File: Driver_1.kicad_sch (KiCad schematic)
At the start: 26 parts

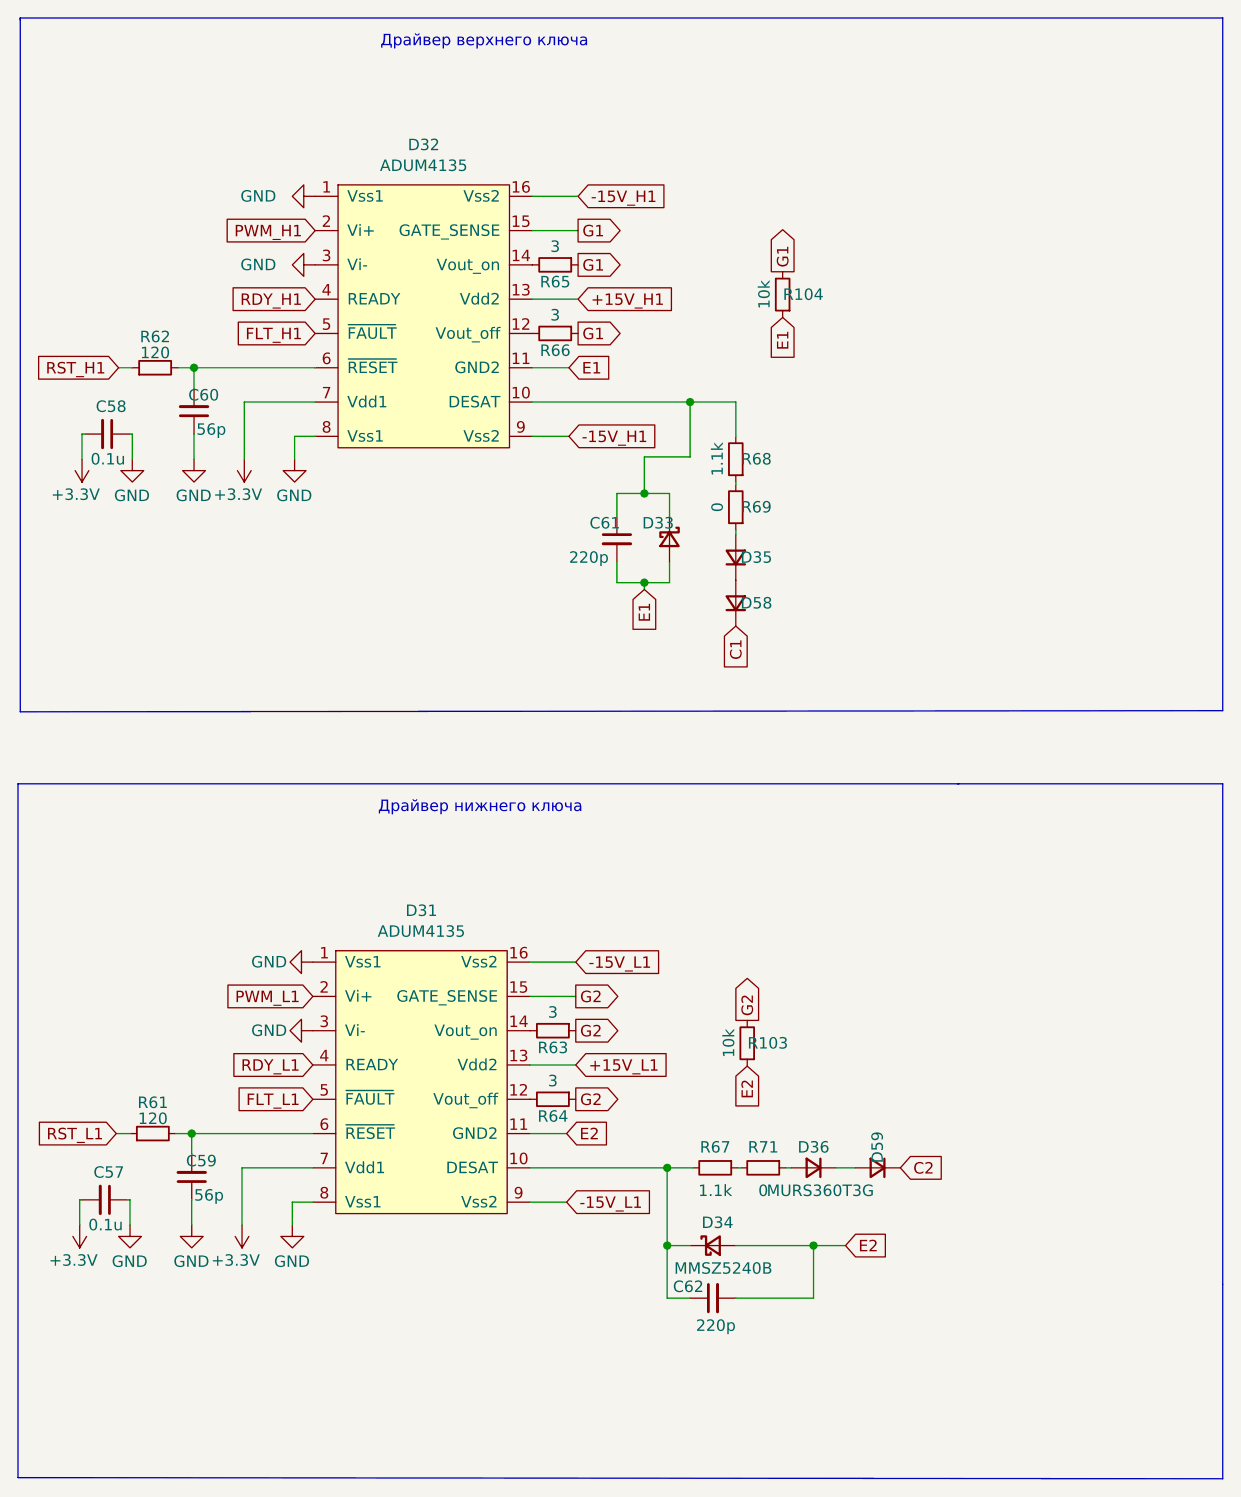
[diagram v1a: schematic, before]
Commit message: Поменял драйвера на китайские
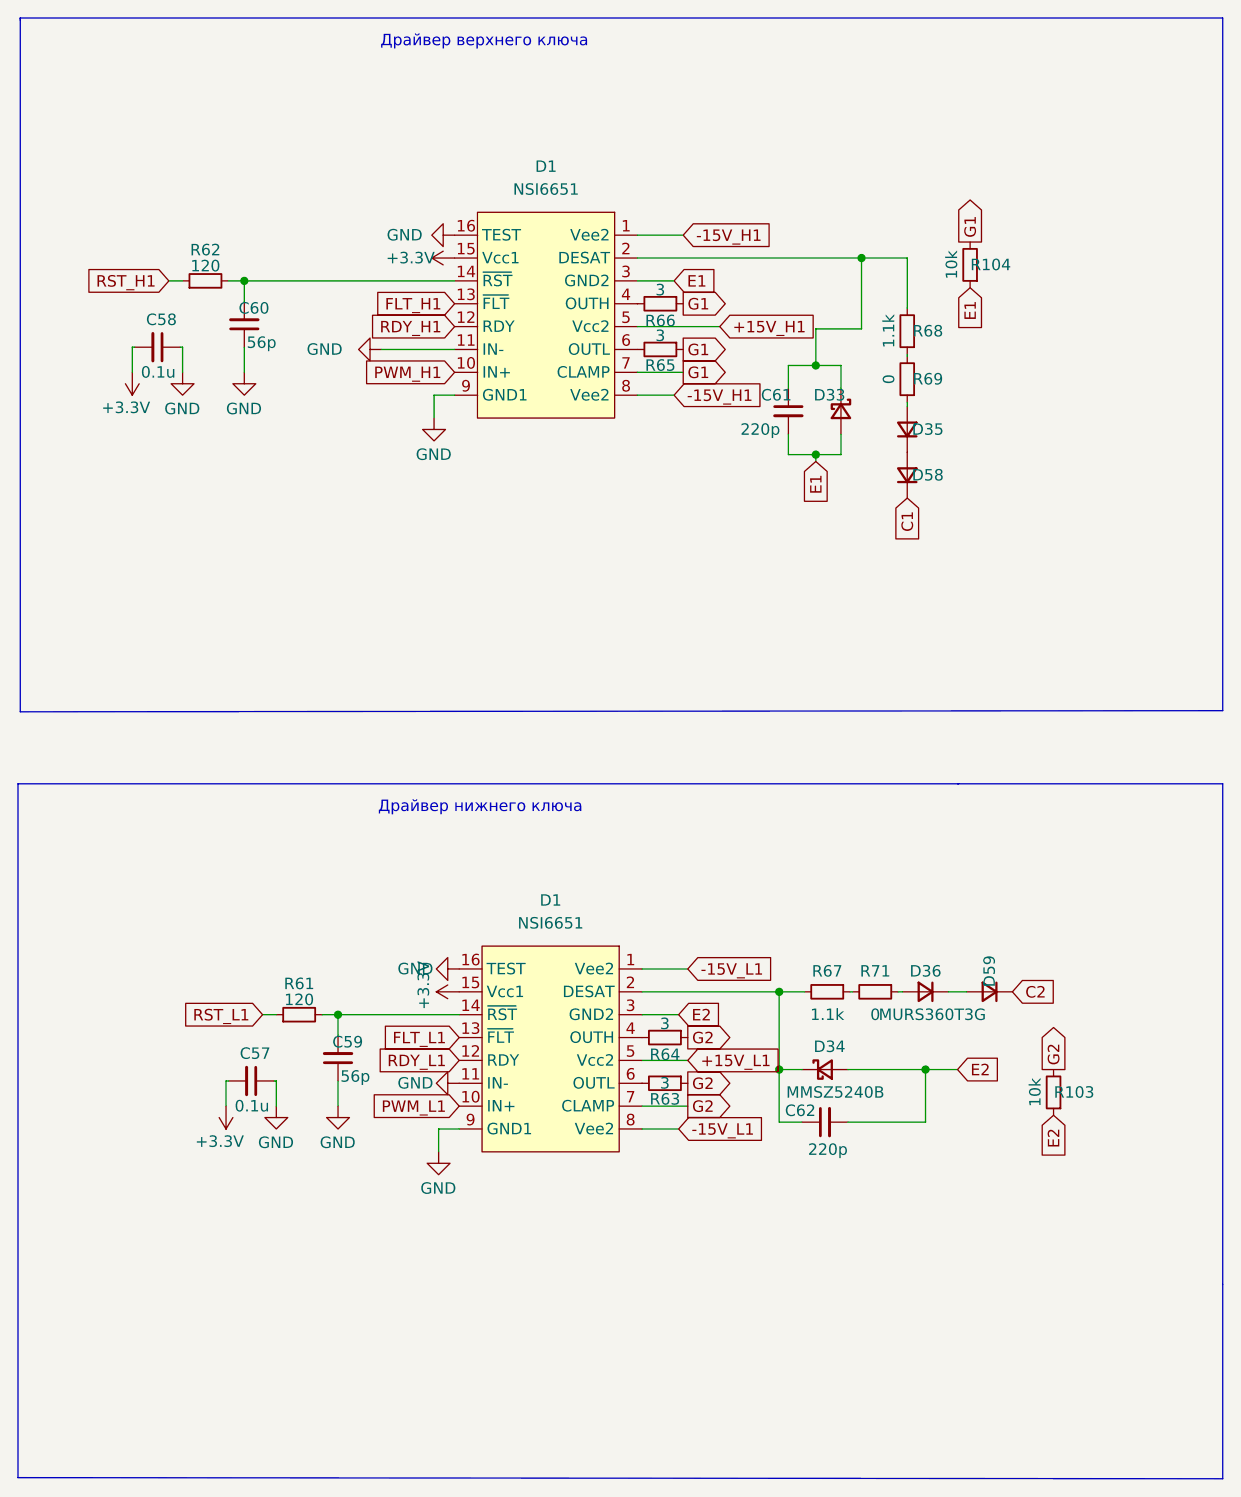
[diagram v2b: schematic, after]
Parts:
- removed D31, D32: ADUM4135, Package_SO:SOIC-16W_7.5x10.3mm_P1.27mm, symbol ADUM_Driver:ADUM4135
- added D1 (x2): NSI6651, Package_SO:SOIC-16W_7.5x10.3mm_P1.27mm, symbol Driver_My:NSI6651
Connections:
- net +15V_H1: now also D1.5 (Vcc2)
- net +15V_L1: now also D1.5 (Vcc2)
- net +3V3: now also D1.15 (Vcc1), D1.15 (Vcc1)
- net -15V_H1: now also D1.1 (Vee2), D1.8 (Vee2)
- net -15V_L1: now also D1.1 (Vee2), D1.8 (Vee2)
- net E1: now also D1.3 (GND2)
- net E2: now also D1.3 (GND2)
- net FLT_H1: now also D1.13 (~{FLT})
- net FLT_L1: now also D1.13 (~{FLT})
- net G1: now also D1.7 (CLAMP)
- net G2: now also D1.7 (CLAMP)
- net GND: now also D1.11 (IN-), D1.11 (IN-), D1.16 (TEST), D1.16 (TEST), D1.9 (GND1), D1.9 (GND1)
- net PWM_H1: now also D1.10 (IN+)
- net PWM_L1: now also D1.10 (IN+)
- net RDY_H1: now also D1.12 (RDY)
- net RDY_L1: now also D1.12 (RDY)
- net at C59.2, R61.2: now also D1.14 (~{RST})
- net at C62.1, D34.1 (K), R67.2: now also D1.2 (DESAT)
- net at R64.2: now also D1.4 (OUTH)
- net at R63.2: now also D1.6 (OUTL)
- net at C61.1, D33.1 (K), R68.2: now also D1.2 (DESAT)
- net at R66.2: now also D1.4 (OUTH)
- net at R65.2: now also D1.6 (OUTL)
- net at C60.2, R62.2: now also D1.14 (~{RST})
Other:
- moved on the sheet: C57, C58, C59, C60, C61, C62, D33, D34, D35, D36, D58, D59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

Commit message: Изменил схему
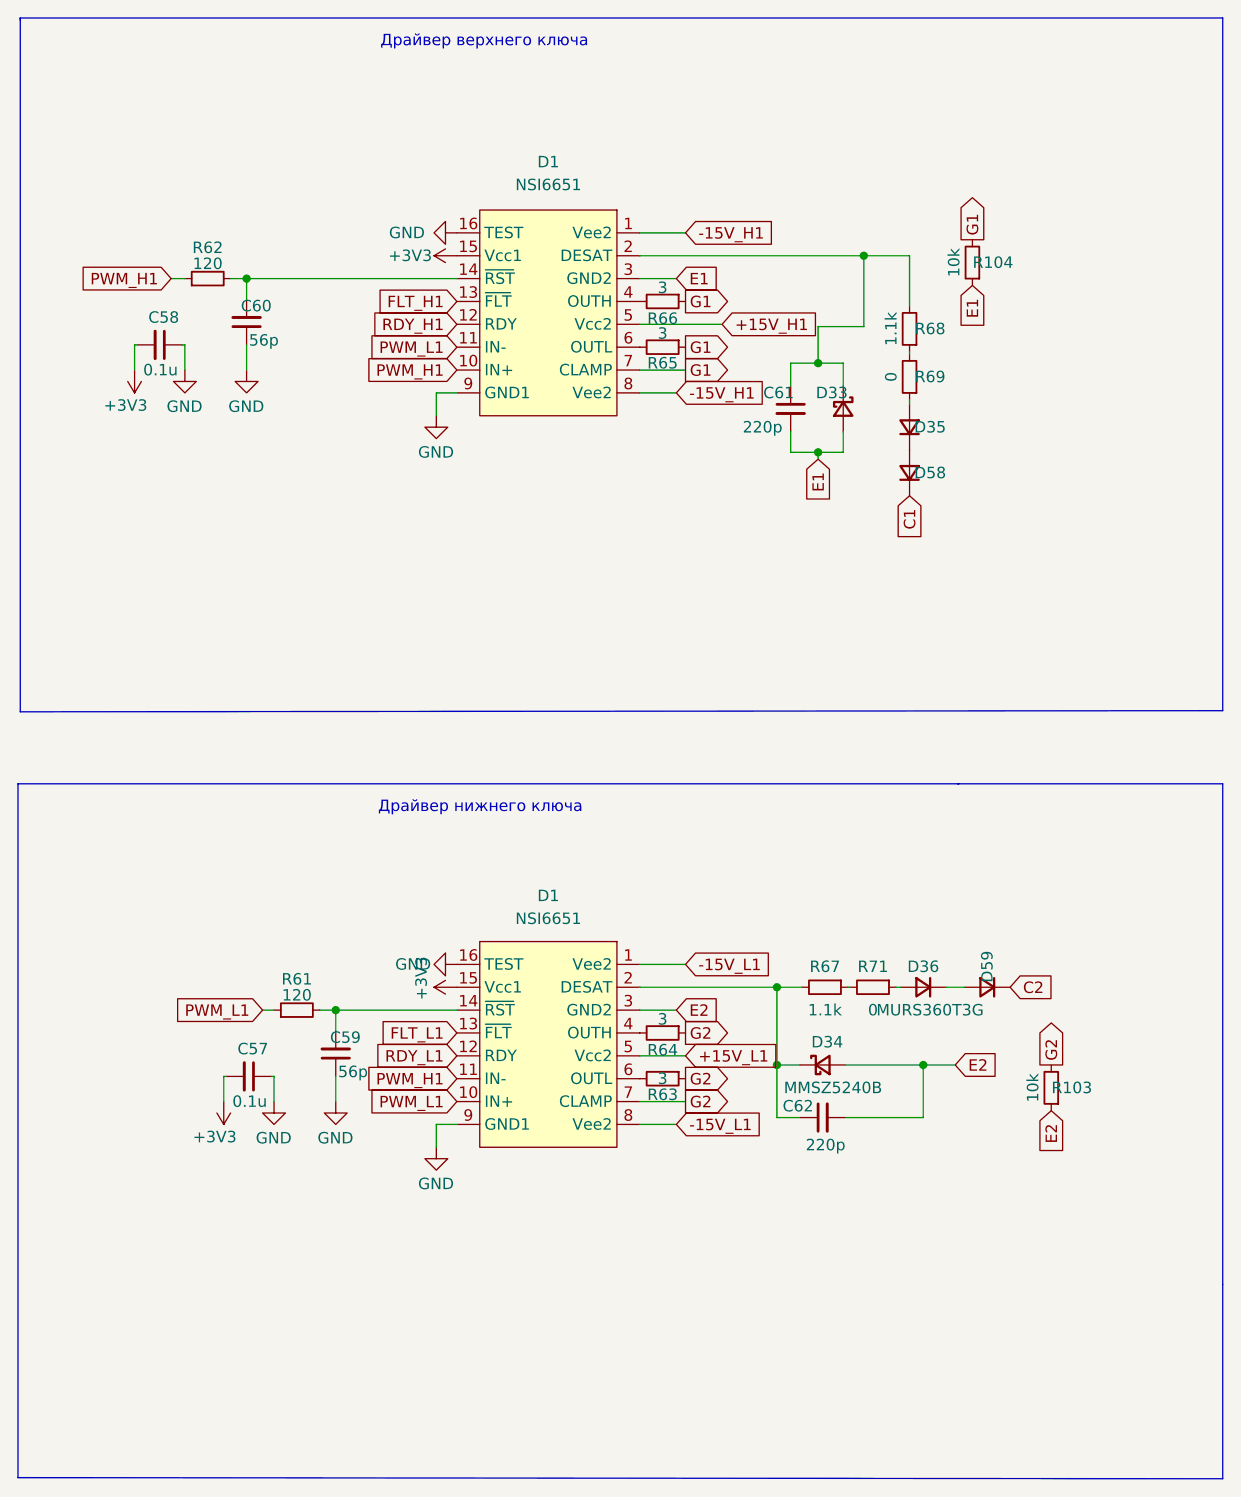
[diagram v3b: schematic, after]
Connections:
- net RST_H1 is gone; now on net PWM_H1: R62.1
- net RST_L1 is gone; now on net PWM_L1: R61.1
- net GND: no longer D1.11 (IN-), D1.11 (IN-)
- net PWM_H1: now also D1.11 (IN-)
- net PWM_L1: now also D1.11 (IN-)
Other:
- moved on the sheet: C57, C59, C62, D1, D34, D36, D59, R103, R61, R63, R64, R67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

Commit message: Разместил все три стойки в своей области
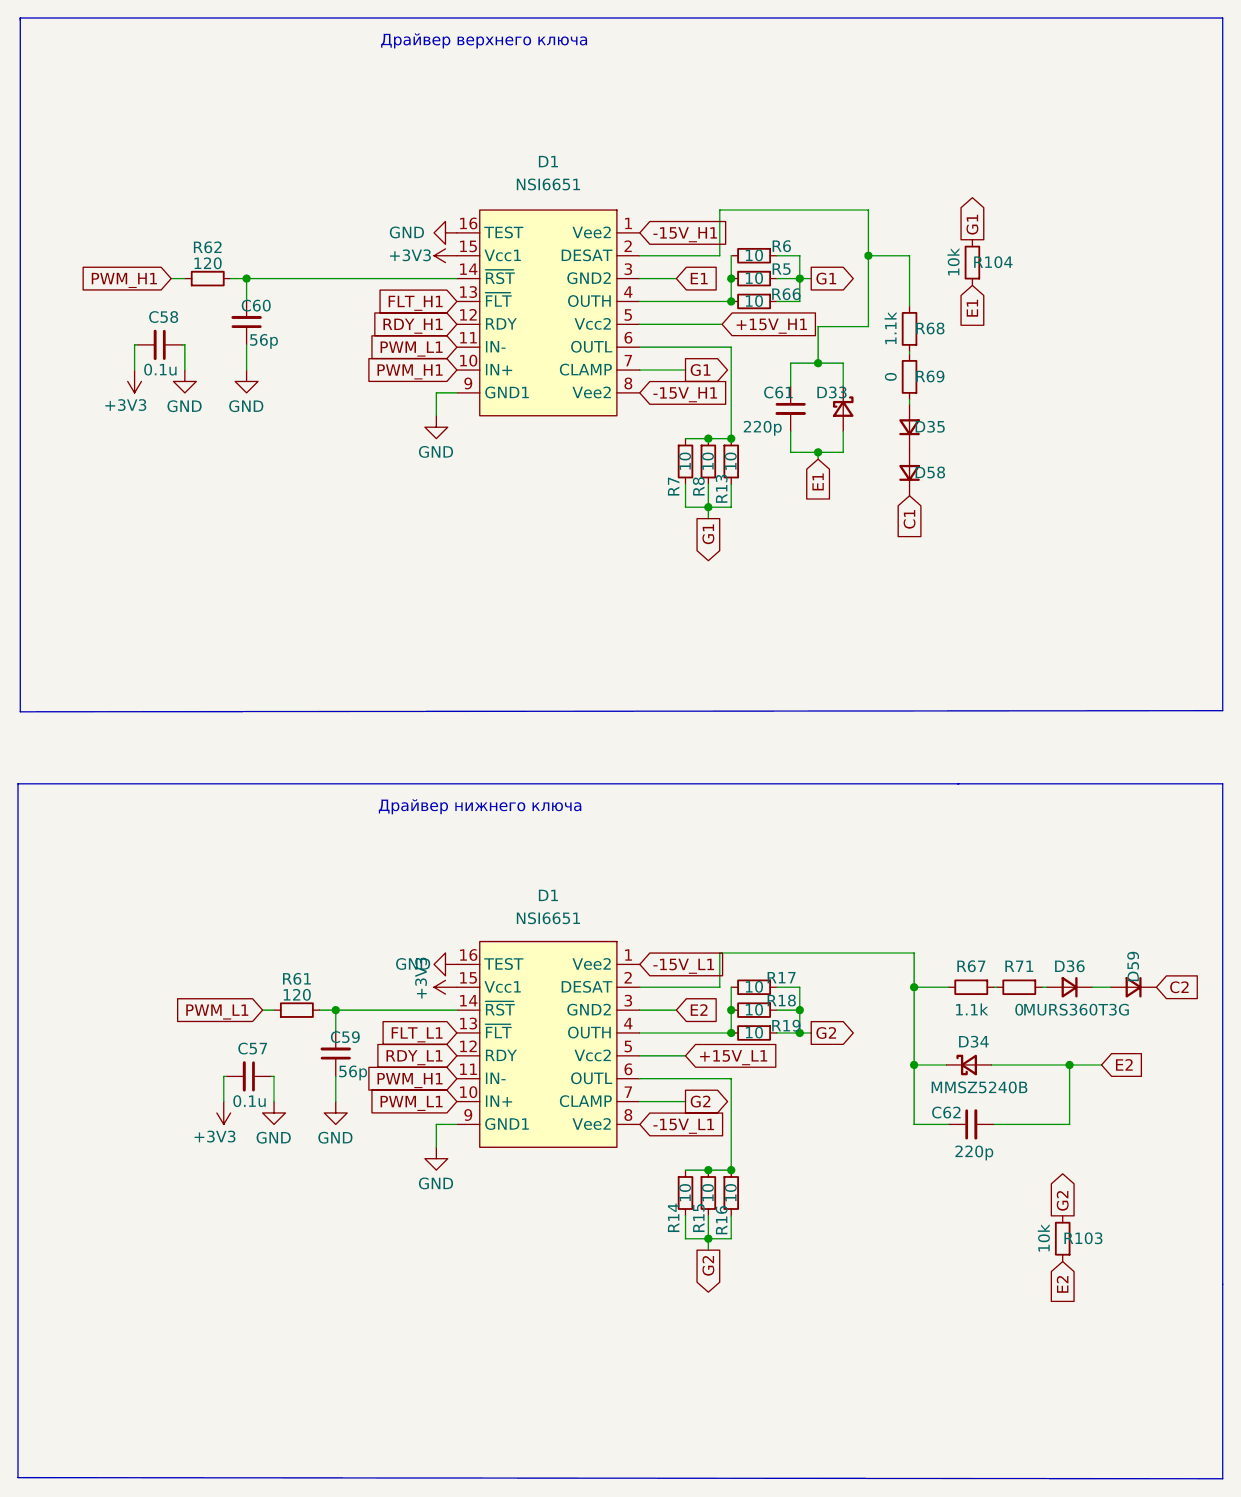
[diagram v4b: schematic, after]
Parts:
- removed R63, R64, R65: 3, Resistor_SMD:R_2512_6332Metric_Pad1.40x3.35mm_HandSolder, symbol Device:R_Small
- added R13, R14, R15, R16, R17, R18, R19, R5, R6, R7, R8: 10, Resistor_SMD:R_1206_3216Metric_Pad1.30x1.75mm_HandSolder, symbol Device:R_Small
- D35, D36, D58, D59: footprint Diode_SMD:D_SMC -> Diode_SMD:D_SMA_Handsoldering
- R66: value 3 -> 10; footprint Resistor_SMD:R_2512_6332Metric_Pad1.40x3.35mm_HandSolder -> Resistor_SMD:R_1206_3216Metric_Pad1.30x1.75mm_HandSolder
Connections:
- net G1: now also R13.2, R5.1, R6.1, R7.2, R8.2
- net G2: now also R14.2, R15.2, R16.2, R17.1, R18.1, R19.1
- net at D1.4 (OUTH), R66.2: now also R5.2, R6.2
- net at D1.6 (OUTL): now also R13.1, R7.1, R8.1
- net at D1.6 (OUTL): now also R14.1, R15.1, R16.1
- net at D1.4 (OUTH): now also R17.2, R18.2, R19.2
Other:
- moved on the sheet: C62, D34, D36, D59, R103, R66, R67, R71

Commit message: Убрал питание 3.3В
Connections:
- net +3V3 renamed +5V
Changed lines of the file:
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@@
 	)
 	(symbol
-		(lib_id "power:+3.3V")
+		(lib_id "power:+5V")
 		(at 80.01 49.53 90)
 		(unit 1)
@@
 		(on_board yes)
 		(dnp no)
-		(property "Reference" "#PWR0168"
+		(property "Reference" "#PWR168"
 			(at 83.82 49.53 0)
 			(effects
@@
 			)
 		)
-		(property "Value" "+3V3"
-			(at 72.39 49.53 90)
-			(effects
-				(font
-					(size 1.27 1.27)
-				)
-				(justify right)
+		(property "Value" "+5V"
+			(at 76.454 49.53 0)
+			(effects
+				(font
+					(size 1.27 1.27)
+				)
 			)
 		)
@@
 			)
 		)
-		(property "Description" ""
+		(property "Description" "Power symbol creates a global label with name \"+5V\""
 			(at 80.01 49.53 0)
 			(effects
@@
 			(project "Adapter"
 				(path "/e63e39d7-6ac0-4ffd-8aa3-1841a4541b55/24ca47b2-866f-4c90-ba1b-98c358d573e6"
-					(reference "#PWR0168")
+					(reference "#PWR168")
 					(unit 1)
 				)
@@
 	)
 	(symbol
-		(lib_id "power:+3.3V")
+		(lib_id "power:+5V")
 		(at 80.01 130.81 90)
 		(unit 1)
@@
 		(on_board yes)
 		(dnp no)
-		(property "Reference" "#PWR0162"
+		(property "Reference" "#PWR162"
 			(at 83.82 130.81 0)
 			(effects
@@
 			)
 		)
-		(property "Value" "+3V3"
-			(at 76.073 127.381 0)
-			(effects
-				(font
-					(size 1.27 1.27)
-				)
-				(justify right)
+		(property "Value" "+5V"
+			(at 76.454 130.81 0)
+			(effects
+				(font
+					(size 1.27 1.27)
+				)
 			)
 		)
@@
 			)
 		)
-		(property "Description" ""
+		(property "Description" "Power symbol creates a global label with name \"+5V\""
 			(at 80.01 130.81 0)
 			(effects
@@
 			(project "Adapter"
 				(path "/e63e39d7-6ac0-4ffd-8aa3-1841a4541b55/24ca47b2-866f-4c90-ba1b-98c358d573e6"
-					(reference "#PWR0162")
+					(reference "#PWR162")
 					(unit 1)
 				)
@@
 	)
 	(symbol
-		(lib_id "power:+3.3V")
+		(lib_id "power:+5V")
 		(at 44.196 62.23 180)
 		(unit 1)
@@
 		(on_board yes)
 		(dnp no)
-		(property "Reference" "#PWR0167"
+		(property "Reference" "#PWR167"
 			(at 44.196 58.42 0)
 			(effects
@@
 			)
 		)
-		(property "Value" "+3V3"
-			(at 40.767 66.167 0)
-			(effects
-				(font
-					(size 1.27 1.27)
-				)
-				(justify right)
+		(property "Value" "+5V"
+			(at 44.196 65.786 0)
+			(effects
+				(font
+					(size 1.27 1.27)
+				)
 			)
 		)
@@
 			)
 		)
-		(property "Description" ""
+		(property "Description" "Power symbol creates a global label with name \"+5V\""
 			(at 44.196 62.23 0)
 			(effects
@@
 			(project "Adapter"
 				(path "/e63e39d7-6ac0-4ffd-8aa3-1841a4541b55/24ca47b2-866f-4c90-ba1b-98c358d573e6"
-					(reference "#PWR0167")
+					(reference "#PWR167")
 					(unit 1)
 				)
@@
 	)
 	(symbol
-		(lib_id "power:+3.3V")
+		(lib_id "power:+5V")
 		(at 54.102 143.51 180)
 		(unit 1)
@@
 		(on_board yes)
 		(dnp no)
-		(property "Reference" "#PWR0161"
+		(property "Reference" "#PWR161"
 			(at 54.102 139.7 0)
 			(effects
@@
 			)
 		)
-		(property "Value" "+3V3"
-			(at 50.673 147.447 0)
-			(effects
-				(font
-					(size 1.27 1.27)
-				)
-				(justify right)
+		(property "Value" "+5V"
+			(at 54.102 147.066 0)
+			(effects
+				(font
+					(size 1.27 1.27)
+				)
 			)
 		)
@@
 			)
 		)
-		(property "Description" ""
+		(property "Description" "Power symbol creates a global label with name \"+5V\""
 			(at 54.102 143.51 0)
 			(effects
@@
 			(project "Adapter"
 				(path "/e63e39d7-6ac0-4ffd-8aa3-1841a4541b55/24ca47b2-866f-4c90-ba1b-98c358d573e6"
-					(reference "#PWR0161")
-					(unit 1)
-				)
+					(reference "#PWR161")
+					(unit 1)
+				)
